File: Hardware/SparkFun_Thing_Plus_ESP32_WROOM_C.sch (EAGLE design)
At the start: 56 parts, among them J3 QWIIC_RIGHT_ANGLE, J6 microSD, Q2 MBT3904DW1T1, Q3 20V/4.2A/52mΩ/1.4W, U1 MCP73831, U2 ESP-WROOM-32NARROW, U3 AP2112K-3.3, U4 MAX17048, U5 AP2112K-3.3, U6 THINGPLUS_LOGICAL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

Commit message: Renamed schematics, replaced parts with sfe lib parts.
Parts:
- removed J6: microSD, SparkFun-Connectors:MICRO-SD-SDIOPUSH-PUSH
- removed U$1: SPARKX-LOGO4, SparkX:SPARKX-LOGO4
- added J2: MICRO-SDFRICTION, SparkFun-Connectors:MICRO-SDFRICTION
- added JP2: JUMPER-SMT_2_NC_TRACE_SILK, SparkFun-Jumpers:JUMPER-SMT_2_NC_TRACE_SILK
- added LOGO1: SFE_LOGO_NAME_FLAME.2_INCH, SparkFun-Aesthetics:SFE_LOGO_NAME_FLAME.2_INCH
- FRAME1: DESIGNER (none) -> Nathan Seidle; REV_BY (none) -> Revised by:; REV_DES (none) -> Alex Brudner
- J3: value QWIIC_RIGHT_ANGLE -> QWIIC_RA
- R3: value 1k -> 150; device SparkFun-Resistors:1KOHM-0402T-1/16W-1% -> SparkFun-Resistors:150OHM-0603-1/10W-5%
- U1: device SparkFun-PowerIC:MCP73831 -> SparkFun-IC-Power:MCP73831
- U2: value ESP-WROOM-32NARROW -> ESP-WROOM-3232D-NARROW; device SparkFun-RF:ESP-WROOM-32NARROW -> SparkFun-RF:ESP-WROOM-3232D-NARROW
- U3, U5: value AP2112K-3.3 -> XC6222B331MR-G; device SparkFun-IC-Power:V_REG_AP2112K-3.3V -> SparkFun-IC-Power:XC6222B331MR-G; PROD_ID VREG-12457 -> (none)
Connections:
- net CHG renamed N$7
- removed net ESP_19/TP_CIPO: J6.DAT0/SDO, U2.MISO3/IO19, U6.CIPO
- removed net ESP_23/TP_COPI: J6.CMD/SDI, U2.MOSI3/IO23, U6.COPI
- new net ESP_19/TP_POCI: J2.DAT0/SDO, U2.MISO3/IO19, U6.CIPO
- new net ESP_23/TP_PICO: J2.CMD/SDI, U2.MOSI3/IO23, U6.COPI
- new net N$4: JP2.1, R3.1
- net 3.3V: now also J2.VCC; no longer J6.VCC
- net ESP_18/TP_SCK: now also J2.CLK/SCK; no longer J6.CLK/SCK
- net ESP_5/SD_CS: now also J2.DAT3/!CS!; no longer J6.DAT3/!CS!
- net GND: now also J2.GND; no longer J6.GND, J6.SHIELD
- net V_USB: now also JP2.2; no longer R3.1
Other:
- note added: "700mA out"
- note added: "700mA out 6V max in"
- note added: "Espressif ESP32-WROOM"
- note added: "v40"
- note removed: "600mA out"
- note removed: "600mA out 6V max in"
- note removed: "Espressif ESP32"
- note removed: "v30"
- moved on the sheet: C1, C10, C15, C19, C2, C3, C4, C5, C6, C7, D1, D12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

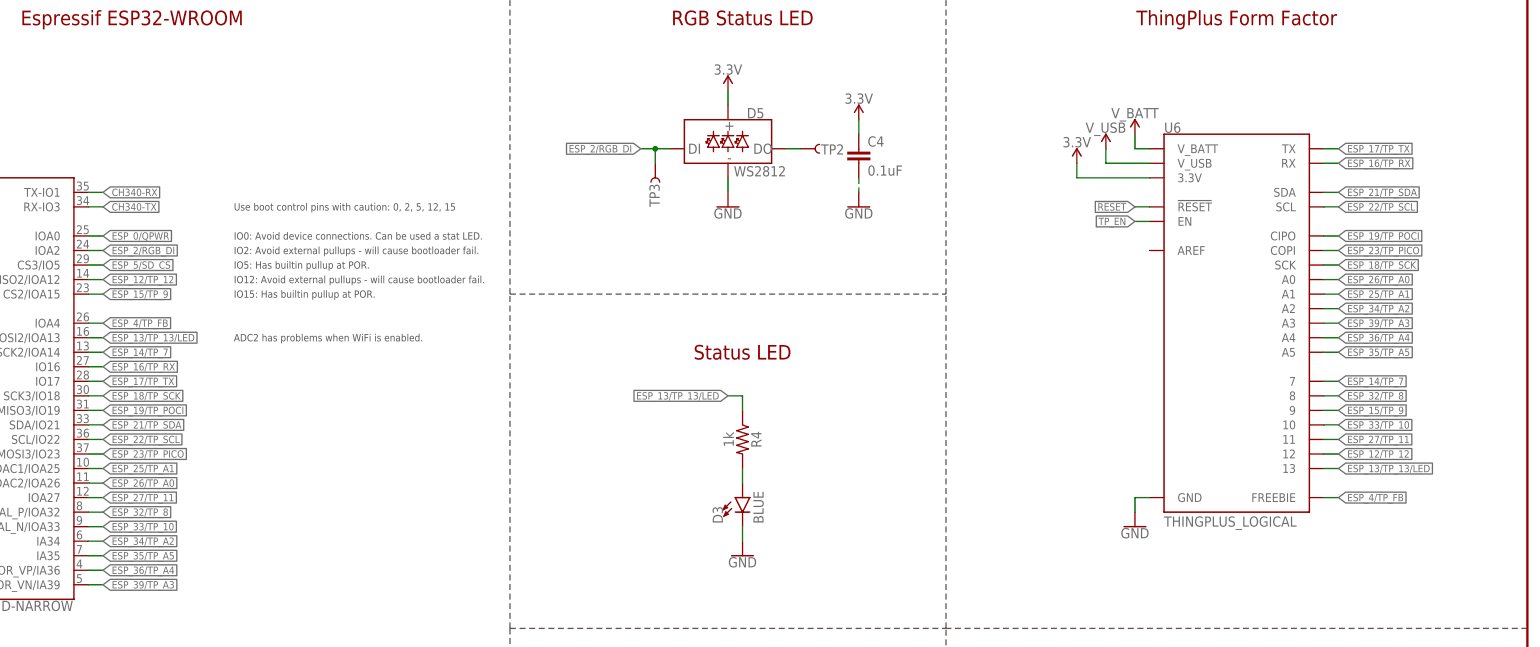
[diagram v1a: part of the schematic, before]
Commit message: All parts are now from SFE libs.
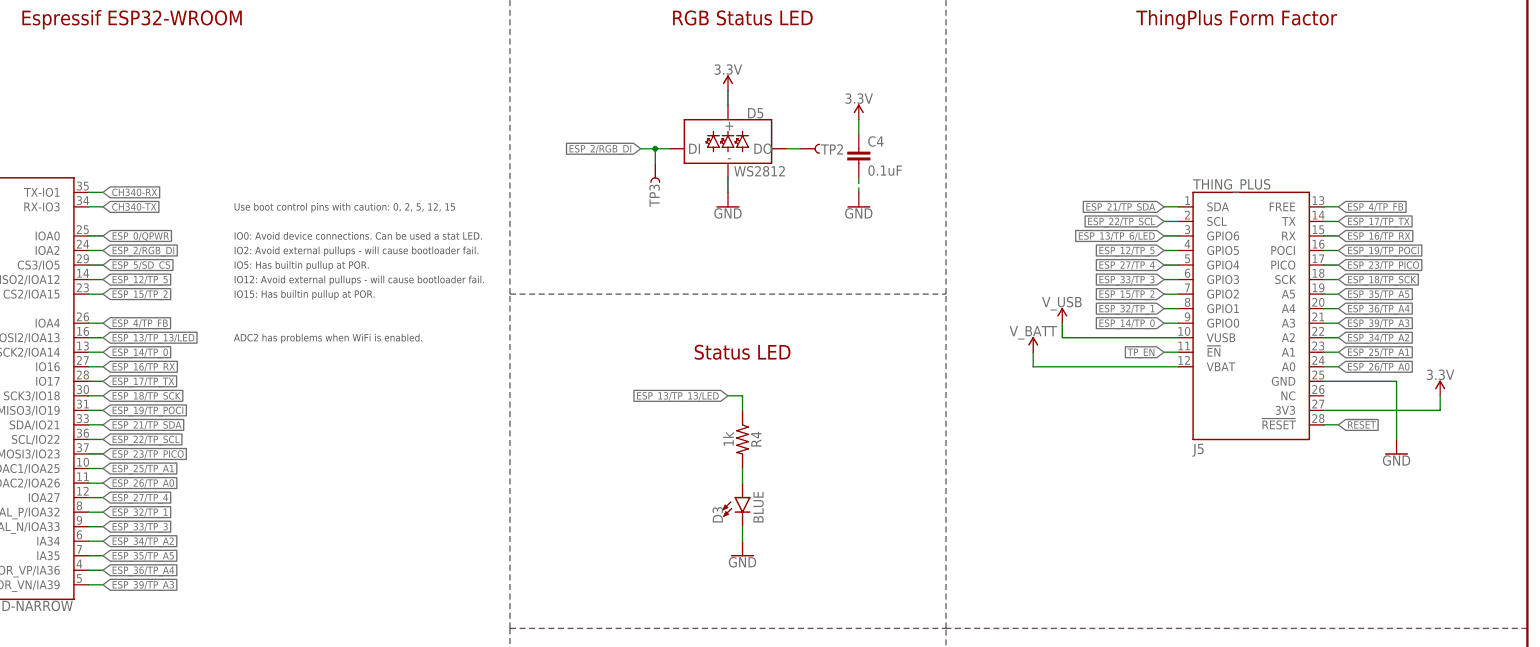
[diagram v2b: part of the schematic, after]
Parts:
- removed U6: THINGPLUS_LOGICAL, ThingPlus:THINGPLUS_LOGICAL
- added J5: THING_PLUS, SparkFun-Boards:THING_PLUS
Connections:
- removed net ESP_12/TP_12: U2.MISO2/IOA12, U6.12
- removed net ESP_14/TP_7: U2.SCK2/IOA14, U6.7
- removed net ESP_15/TP_9: U2.CS2/IOA15, U6.9
- removed net ESP_27/TP_11: U2.IOA27, U6.11
- removed net ESP_32/TP_8: U2.XTAL_P/IOA32, U6.8
- removed net ESP_33/TP_10: U2.XTAL_N/IOA33, U6.10
- new net ESP_12/TP_5: J5.GPIO5, U2.MISO2/IOA12
- new net ESP_13/TP_6/LED: J5.GPIO6
- new net ESP_14/TP_0: J5.GPIO0, U2.SCK2/IOA14
- new net ESP_15/TP_2: J5.GPIO2, U2.CS2/IOA15
- new net ESP_27/TP_4: J5.GPIO4, U2.IOA27
- new net ESP_32/TP_1: J5.GPIO1, U2.XTAL_P/IOA32
- new net ESP_33/TP_3: J5.GPIO3, U2.XTAL_N/IOA33
- net !RESET!: now also J5.!RESET; no longer U6.!RESET
- net 3.3V: now also J5.3V3; no longer U6.3.3V
- net ESP_13/TP_13/LED: no longer U6.13
- net ESP_16/TP_RX: now also J5.RX; no longer U6.RX
- net ESP_17/TP_TX: now also J5.TX; no longer U6.TX
- net ESP_18/TP_SCK: now also J5.SCK; no longer U6.SCK
- net ESP_19/TP_POCI: now also J5.POCI; no longer U6.CIPO
- net ESP_21/TP_SDA: now also J5.SDA; no longer U6.SDA
- net ESP_22/TP_SCL: now also J5.SCL; no longer U6.SCL
- net ESP_23/TP_PICO: now also J5.PICO; no longer U6.COPI
- net ESP_25/TP_A1: now also J5.A1; no longer U6.A1
- net ESP_26/TP_A0: now also J5.A0; no longer U6.A0
- net ESP_34/TP_A2: now also J5.A2; no longer U6.A2
- net ESP_35/TP_A5: now also J5.A5; no longer U6.A5
- net ESP_36/TP_A4: now also J5.A4; no longer U6.A4
- net ESP_39/TP_A3: now also J5.A3; no longer U6.A3
- net ESP_4/TP_FB: now also J5.FREE; no longer U6.FREEBIE
- net GND: now also J5.GND; no longer U6.GND
- net TP_EN: now also J5.!EN; no longer U6.EN
- net V_BATT: now also J5.VBAT; no longer U6.V_BATT
- net V_USB: now also J5.VUSB; no longer U6.V_USB

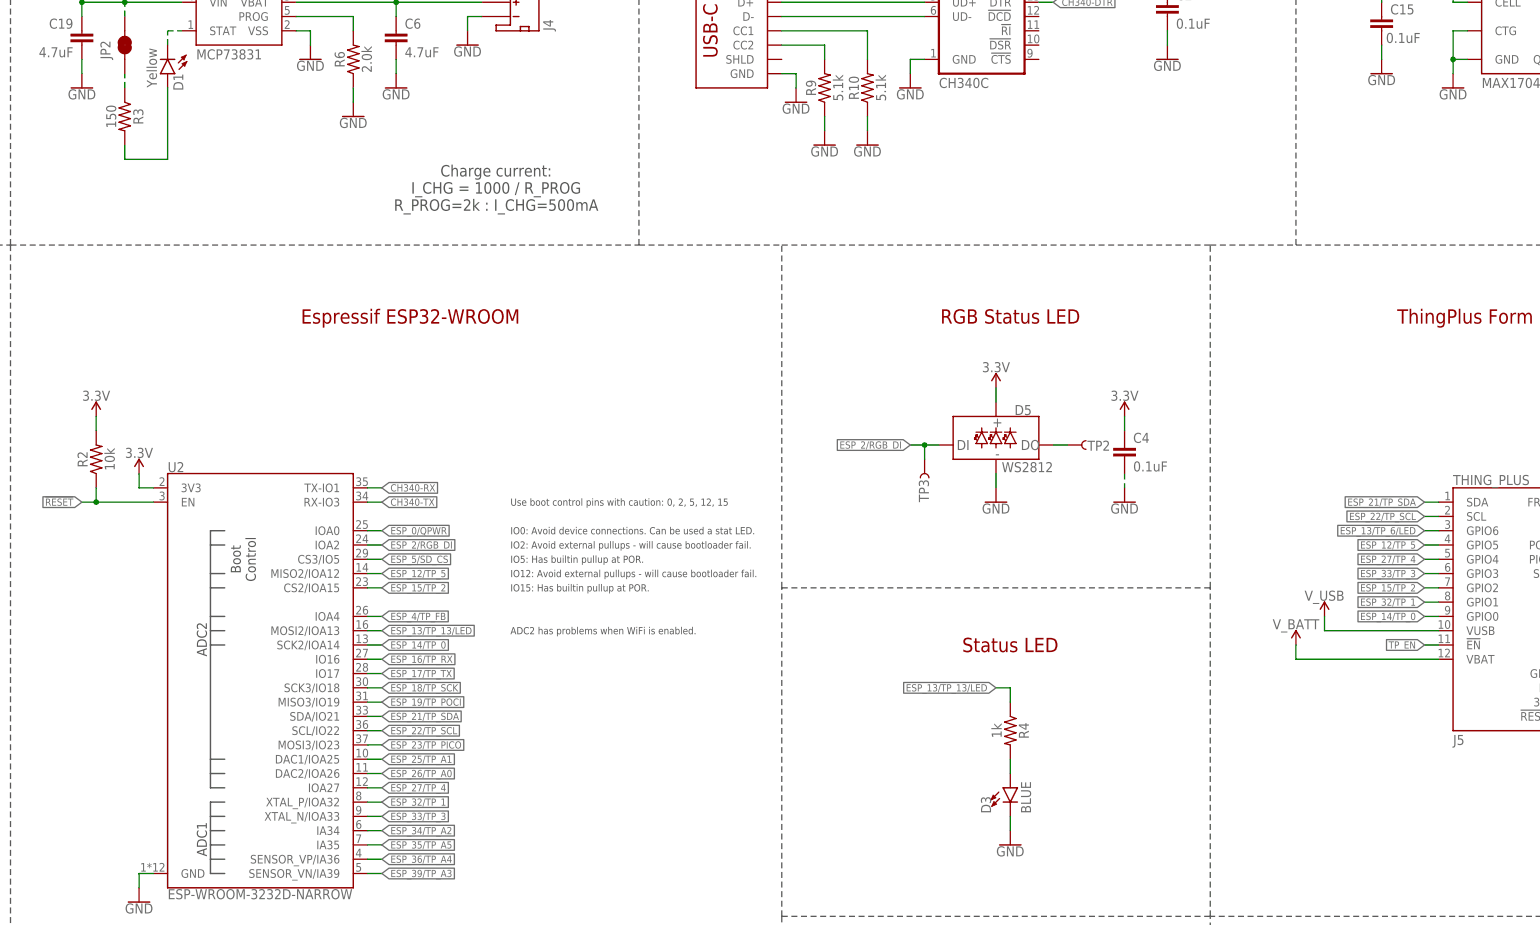
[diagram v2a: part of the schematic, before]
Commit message: Placed all new components, pinned out PTHs.
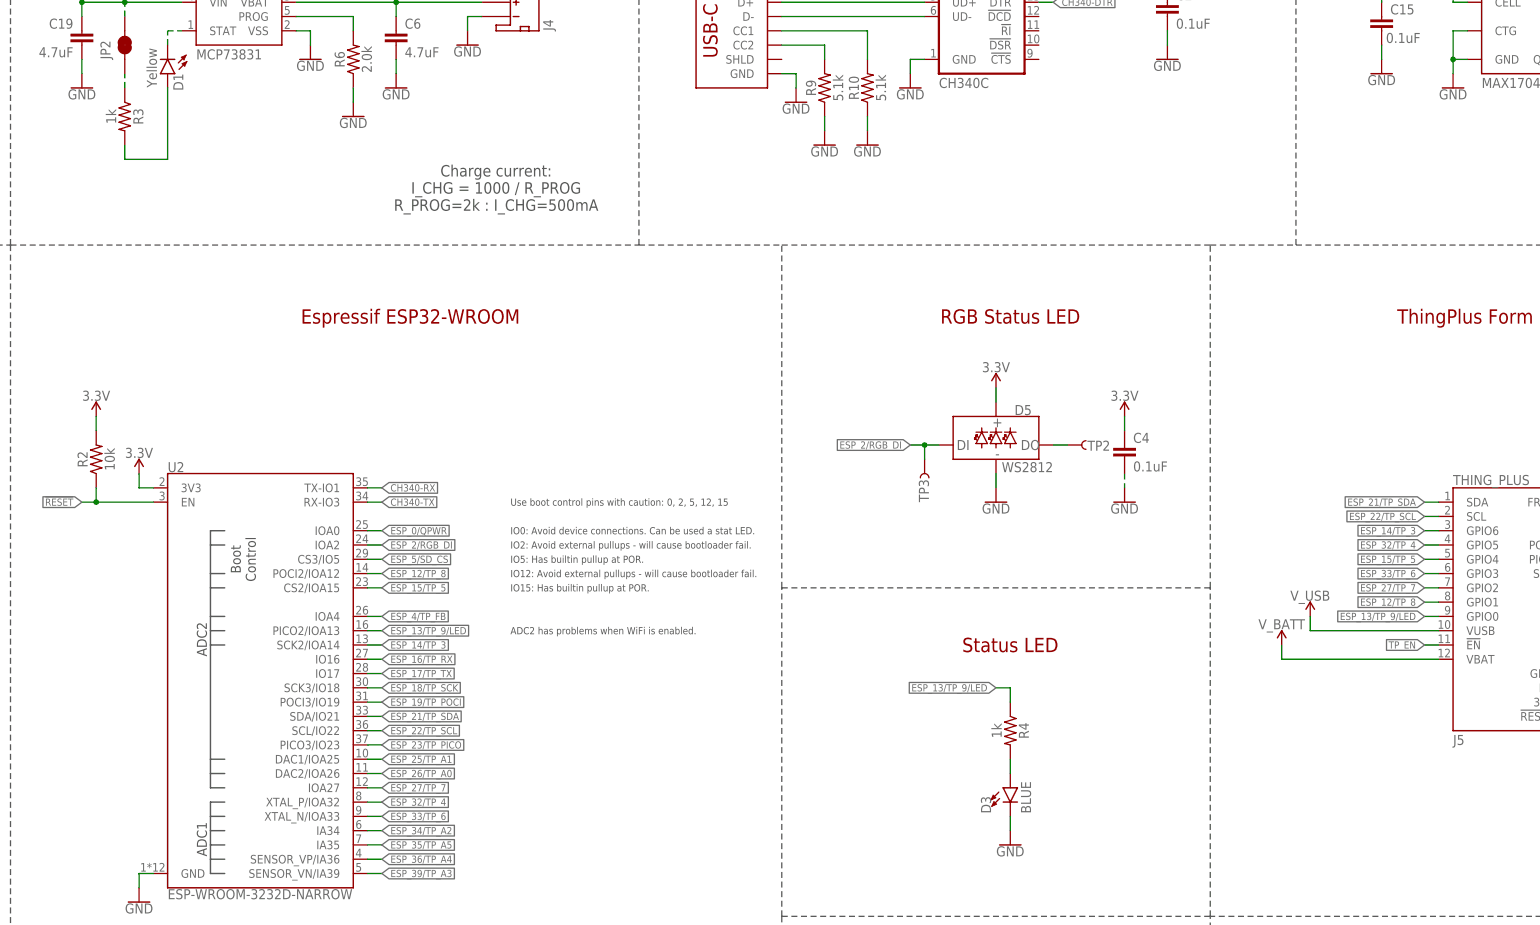
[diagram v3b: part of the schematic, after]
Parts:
- R3: value 150 -> 1k; device SparkFun-Resistors:150OHM-0603-1/10W-5% -> SparkFun-Resistors:1KOHM-0402T-1/16W-1%
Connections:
- net ESP_33/TP_3 renamed ESP_33/TP_6
- removed net ESP_12/TP_5: J5.GPIO5, U2.MISO2/IOA12
- removed net ESP_13/TP_13/LED: R4.1, U2.MOSI2/IOA13
- removed net ESP_13/TP_6/LED: J5.GPIO6
- removed net ESP_14/TP_0: J5.GPIO0, U2.SCK2/IOA14
- removed net ESP_15/TP_2: J5.GPIO2, U2.CS2/IOA15
- removed net ESP_27/TP_4: J5.GPIO4, U2.IOA27
- removed net ESP_32/TP_1: J5.GPIO1, U2.XTAL_P/IOA32
- new net ESP_12/TP_8: J5.GPIO1, U2.POCI2/IOA12
- new net ESP_13/TP_9/LED: J5.GPIO0, R4.1, U2.PICO2/IOA13
- new net ESP_14/TP_3: J5.GPIO6, U2.SCK2/IOA14
- new net ESP_15/TP_5: J5.GPIO4, U2.CS2/IOA15
- new net ESP_27/TP_7: J5.GPIO2, U2.IOA27
- new net ESP_32/TP_4: J5.GPIO5, U2.XTAL_P/IOA32
- net ESP_19/TP_POCI: now also U2.POCI3/IO19; no longer U2.MISO3/IO19
- net ESP_23/TP_PICO: now also U2.PICO3/IO23; no longer U2.MOSI3/IO23

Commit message: Completed Board update pre-DR.
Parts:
- LOGO1: value SFE_LOGO_NAME_FLAME.2_INCH -> SFE_LOGO_NAME_FLAME.1_INCH; device SparkFun-Aesthetics:SFE_LOGO_NAME_FLAME.2_INCH -> SparkFun-Aesthetics:SFE_LOGO_NAME_FLAME.1_INCH
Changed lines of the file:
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@@
 <part name="TP3" library="SparkFun-Connectors" deviceset="TEST-POINT" device="3X5" value="TEST-POINT3X5"/>
 <part name="TP4" library="SparkFun-Connectors" deviceset="TEST-POINT" device="3X5" value="TEST-POINT3X5"/>
-<part name="LOGO1" library="SparkFun-Aesthetics" deviceset="SFE_LOGO_NAME_FLAME" device=".2_INCH"/>
+<part name="LOGO1" library="SparkFun-Aesthetics" deviceset="SFE_LOGO_NAME_FLAME" device=".1_INCH" value="SFE_LOGO_NAME_FLAME.1_INCH"/>
 <part name="JP2" library="SparkFun-Jumpers" deviceset="JUMPER-SMT_2_NC_TRACE" device="_SILK" package3d_urn="urn:adsk.eagle:package:39281/1" value=""/>
 <part name="U3" library="SparkFun-IC-Power" deviceset="XC6222" device="B331MR-G"/>

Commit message: Completed updates post DR.
Schematic:
Change all  text to vector, 8%
Add row lines to boot mode table
Add NC jumper on USB-C shield.
Change 0.1u cap to 10u next to uSD.
Update uSD device to pull in newest changes to keepout.
Label LED jumpers JP1, JP2
Change ADC2 note to say “Is not available when wifi enabled.”
Rearrange schematic to make ESP32 notes fit in box when vectored font.
Change symbol for SOT-25 VREGs to remove NC pin.
Add Nate’s Thing Plus symbol to the SFE libs and make the board change to be logical instead of physical.

Board:
Space out top RGB LED per Dryw’s design
Add dimensions to the uSD card and it’s protrusion.
Add pin 1 indicator for CH340, it’s covered.
Add designed/revised by to board.
Move C19 close to batt charge IC, remove top silk on EN/VB to make it fit if necessary.
Change the width of V_USB to be consistent across the board.
Aim for 30 mil, that’s a 60deg increase at 2A
Got 22 mil all around, best I could do
Change GND, 3.3, NC bottom silk to be pill-style
Fit a flame logo on top.
Acid traps
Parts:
- added JP3: JUMPER-SMT_2_NC_TRACE_SILK, SparkFun-Jumpers:JUMPER-SMT_2_NC_TRACE_SILK
- C5: value 0.1uF -> 10uF; device SparkFun-Capacitors:0.1UF-0402T-6.3V-10%-X7R -> SparkFun-Capacitors:10UF-0402T-6.3V-20%
- J5: value THING_PLUS -> THING_PLUS_LOGICAL; device SparkFun-Boards:THING_PLUS -> SparkFun-Boards:THING_PLUS_LOGICAL
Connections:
- net ESP_12/TP_8 renamed ESP_12/GPIO1
- net ESP_13/TP_9/LED renamed ESP_13/GPIO0/LED
- net ESP_14/TP_3 renamed ESP_14/GPIO6
- net ESP_15/TP_5 renamed ESP_15/GPIO4
- net ESP_27/TP_7 renamed ESP_27/GPIO2
- net ESP_32/TP_4 renamed ESP_32/GPIO5
- net ESP_33/TP_6 renamed ESP_33/GPIO3
- new net N$8: J1.SHLD, JP3.2
- net !RESET!: now also Q2G1.C; no longer Q2Q1.C
- net 3.3V: now also J5.3.3V; no longer J5.3V3
- net CH340-DTR: now also Q2G2.E; no longer Q2Q2.E
- net CH340-RTS: now also Q2G1.E; no longer Q2Q1.E
- net DTR-10K: now also Q2G1.B; no longer Q2Q1.B
- net ESP_0/QPWR: now also Q2G2.C; no longer Q2Q2.C
- net ESP_4/TP_FB: now also J5.FREEBIE; no longer J5.FREE
- net GND: now also JP3.1
- net RTS-10K: now also Q2G2.B; no longer Q2Q2.B
- net TP_EN: now also J5.EN; no longer J5.!EN
- net V_BATT: now also J5.V_BATT; no longer J5.VBAT
- net V_USB: now also J5.V_USB; no longer J5.VUSB
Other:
- note added: "ADC2 is unavailable when WiFi is enabled."
- note added: "CHG"
- note added: "PWR"
- note removed: "ADC2 has problems when WiFi is enabled."
- moved on the sheet: C2, C4, D3, D5, R10, R4, R9, S3, S4, TP1, TP2, TP3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

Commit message: Update post DR changes.
Minor movement edits.
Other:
- note added: "Cut trace to disconnect CHG LED."
- note added: "Cut trace to disconnect PWR LED."
- note added: "Cut trace to disconnect SHLD from GND."
- note removed: "CHG"
- note removed: "PWR"
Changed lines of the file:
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@@
 <wire x1="30.48" y1="158.75" x2="86.36" y2="158.75" width="0.2032" layer="97"/>
 <wire x1="30.48" y1="156.21" x2="86.36" y2="156.21" width="0.2032" layer="97"/>
-<text x="139.192" y="241.554" size="1.778" layer="97" font="vector">CHG</text>
-<text x="109.22" y="252.984" size="1.778" layer="97" font="vector">PWR</text>
+<text x="126.492" y="211.074" size="1.778" layer="97" font="vector">Cut trace to
+disconnect CHG LED.</text>
+<text x="73.66" y="258.064" size="1.778" layer="97" font="vector">Cut trace to
+disconnect PWR LED.</text>
+<text x="235.712" y="211.074" size="1.778" layer="97" font="vector">Cut trace to
+disconnect SHLD from GND.</text>
 </plain>
 <instances>

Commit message: Added 7-bit I2C address text.
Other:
- note added: "Unshifted 7-bit I2C address: 0x36"
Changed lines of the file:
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@@
 <text x="235.712" y="211.074" size="1.778" layer="97" font="vector">Cut trace to
 disconnect SHLD from GND.</text>
+<text x="360.68" y="220.98" size="1.778" layer="97" font="vector">Unshifted 7-bit I2C address: 0x36</text>
 </plain>
 <instances>
